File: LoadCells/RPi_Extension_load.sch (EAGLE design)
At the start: 42 parts, among them U1 AD7730BRUZ, U2 AD7730BRUZ, U3 AD7730BRUZ, U4 AD7730BRUZ, U5 AD7730BRUZ, U6 AD7730BRUZ, U7 AD7730BRUZ, U8 AD7730BRUZ, U9 STM32F103RCT6, Y1 ABM3B, Y2 KC2520B-C1

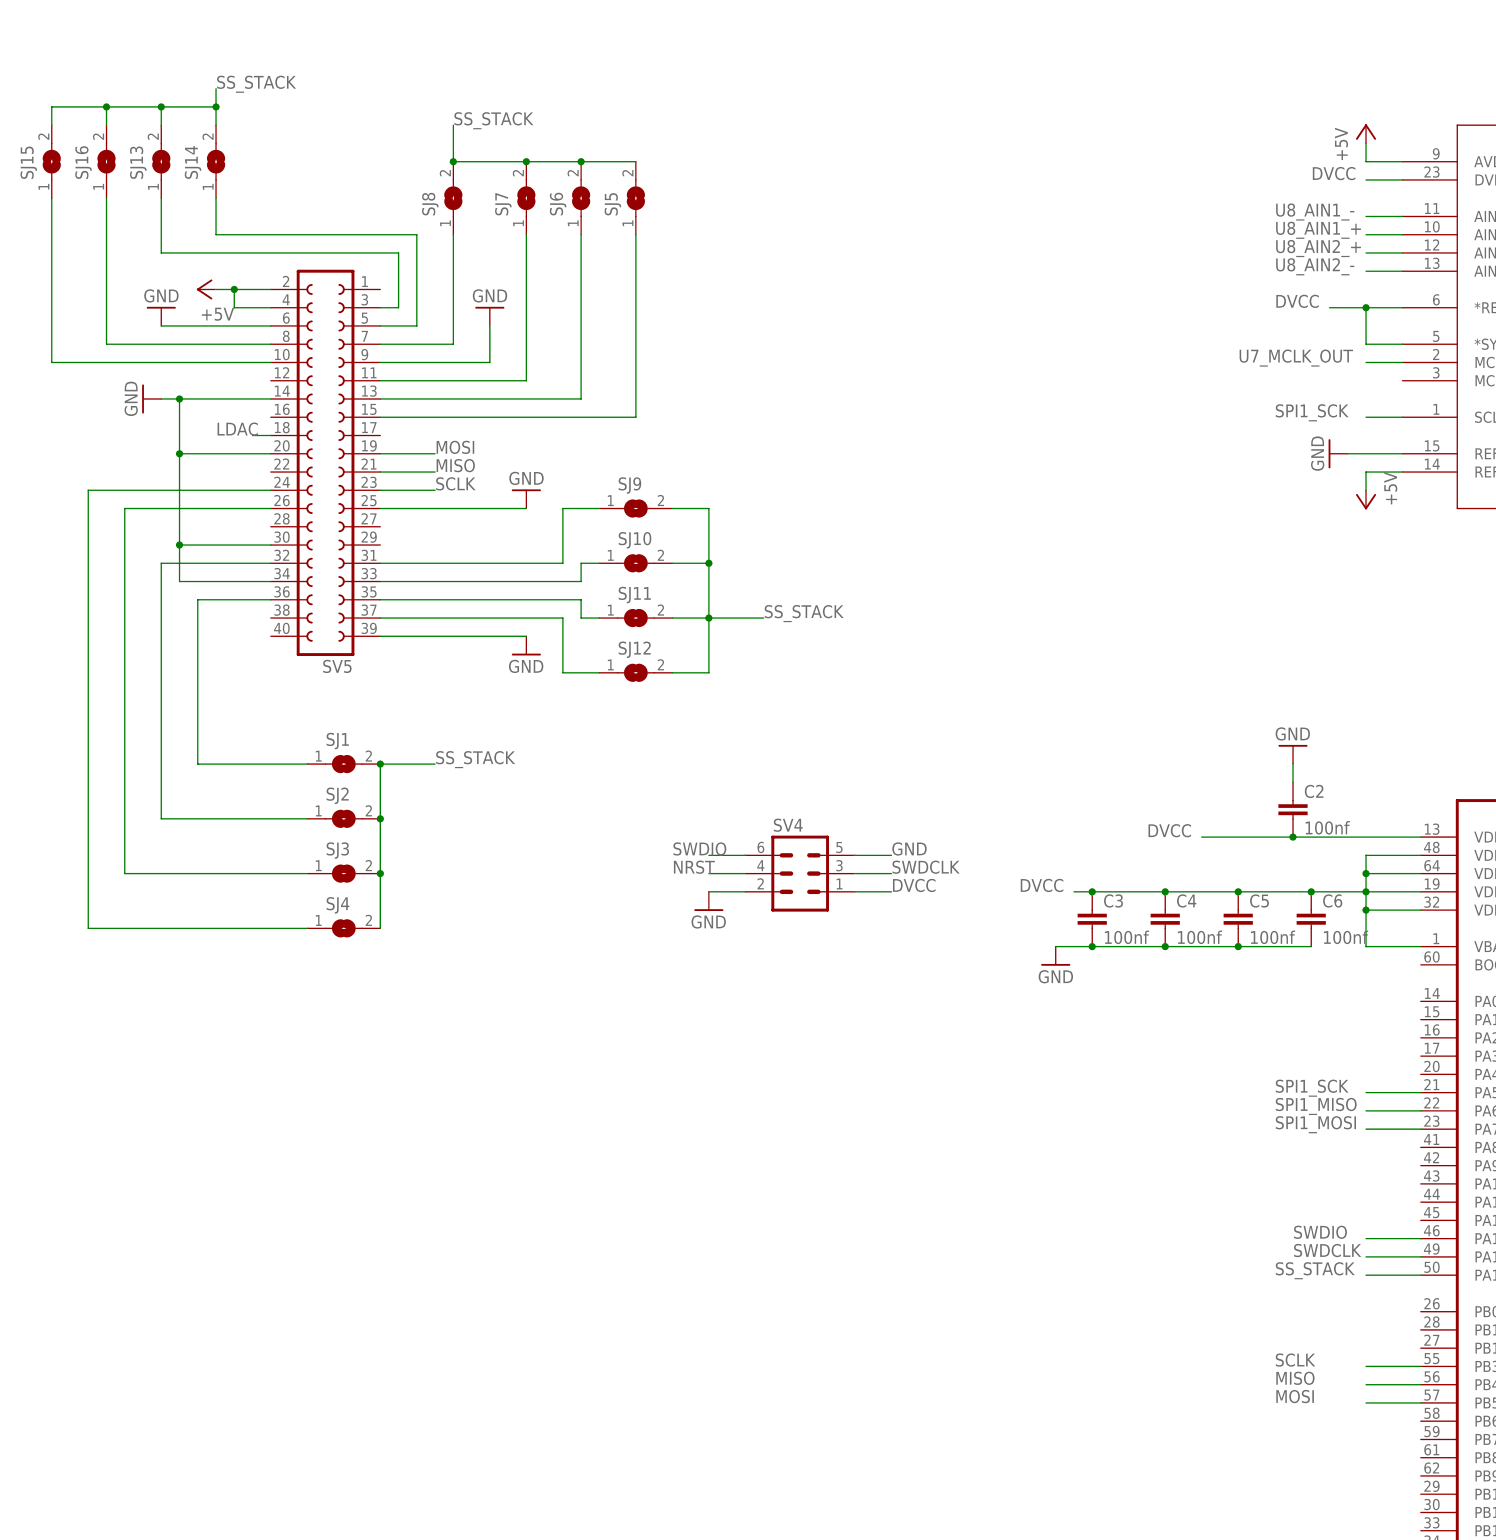
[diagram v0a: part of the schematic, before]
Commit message: cleaned up silklayer of load cell board
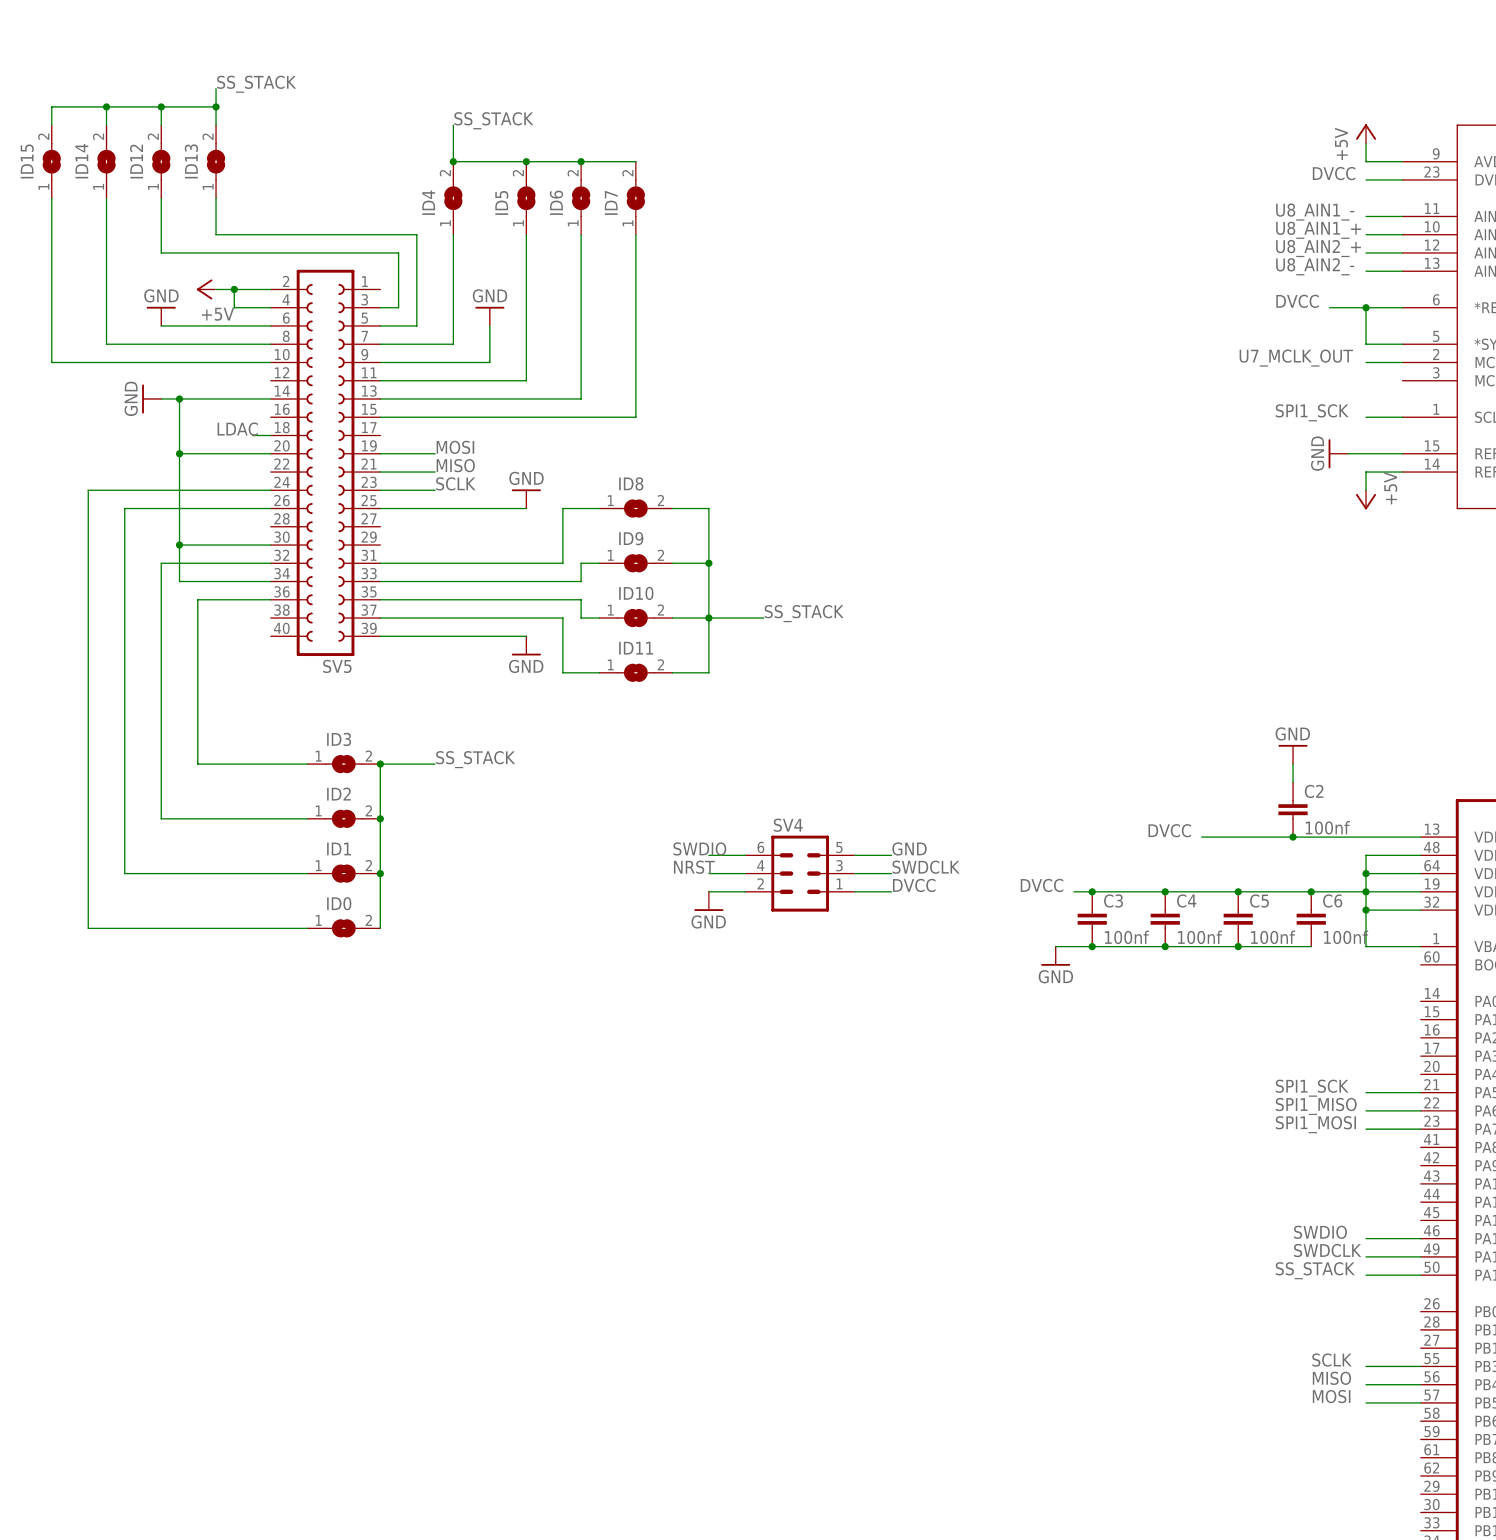
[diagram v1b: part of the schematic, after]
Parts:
- renumbered SJ1 to ID3, SJ10 to ID9, SJ11 to ID10, SJ12 to ID11, SJ13 to ID12, SJ14 to ID13, SJ15 to ID15, SJ16 to ID14, SJ2 to ID2, SJ3 to ID1, SJ4 to ID0, SJ5 to ID7, SJ6 to ID6, SJ7 to ID5, SJ8 to ID4, SJ9 to ID8
